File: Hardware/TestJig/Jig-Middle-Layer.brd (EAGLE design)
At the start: 62.2 x 54.6 mm, 8 parts

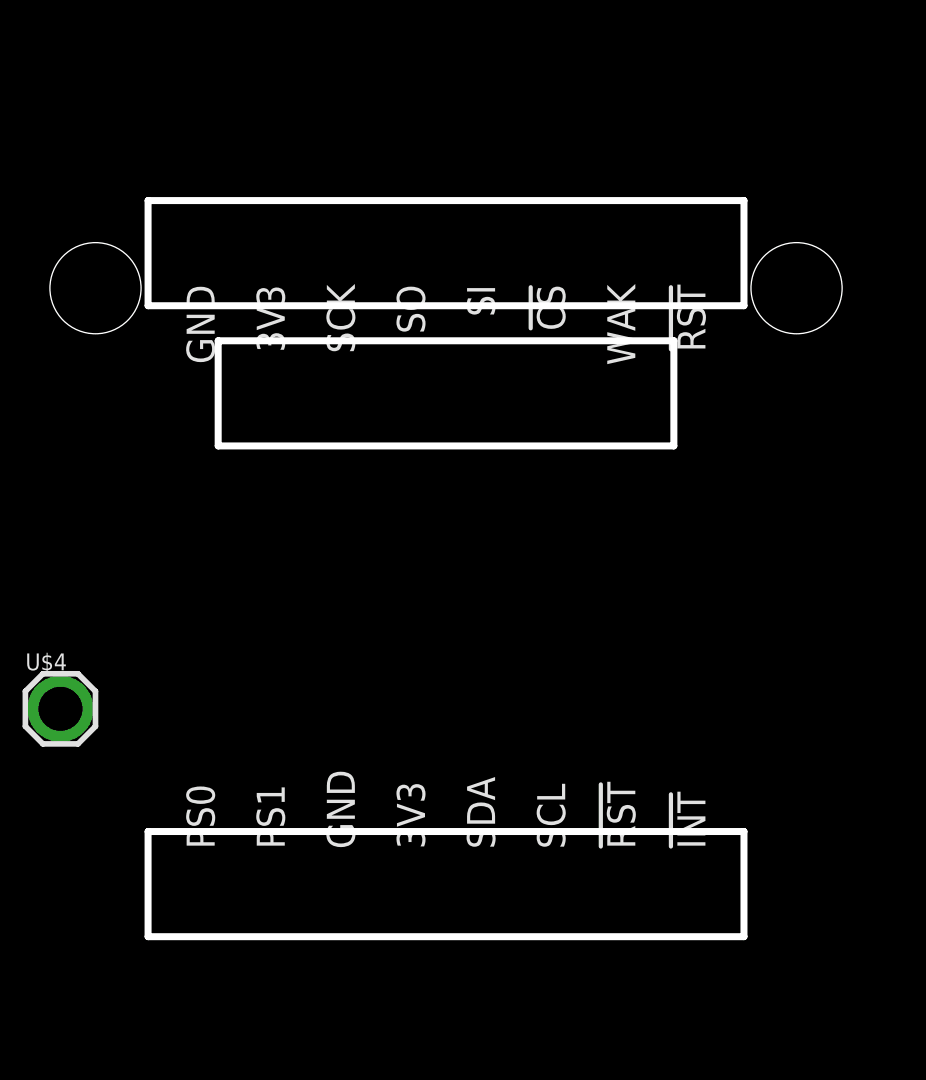
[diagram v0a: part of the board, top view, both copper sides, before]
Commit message: fixed white wires on lower layer, added pass throughs for pogo
replaced white wires with bottom traces. 3  traces:  A4, A5, CS

added PTH holes with 1.45mm diameter, giving .15mm clearance of the pogo pin head.

removed cutouts so PCBs can be fabricated
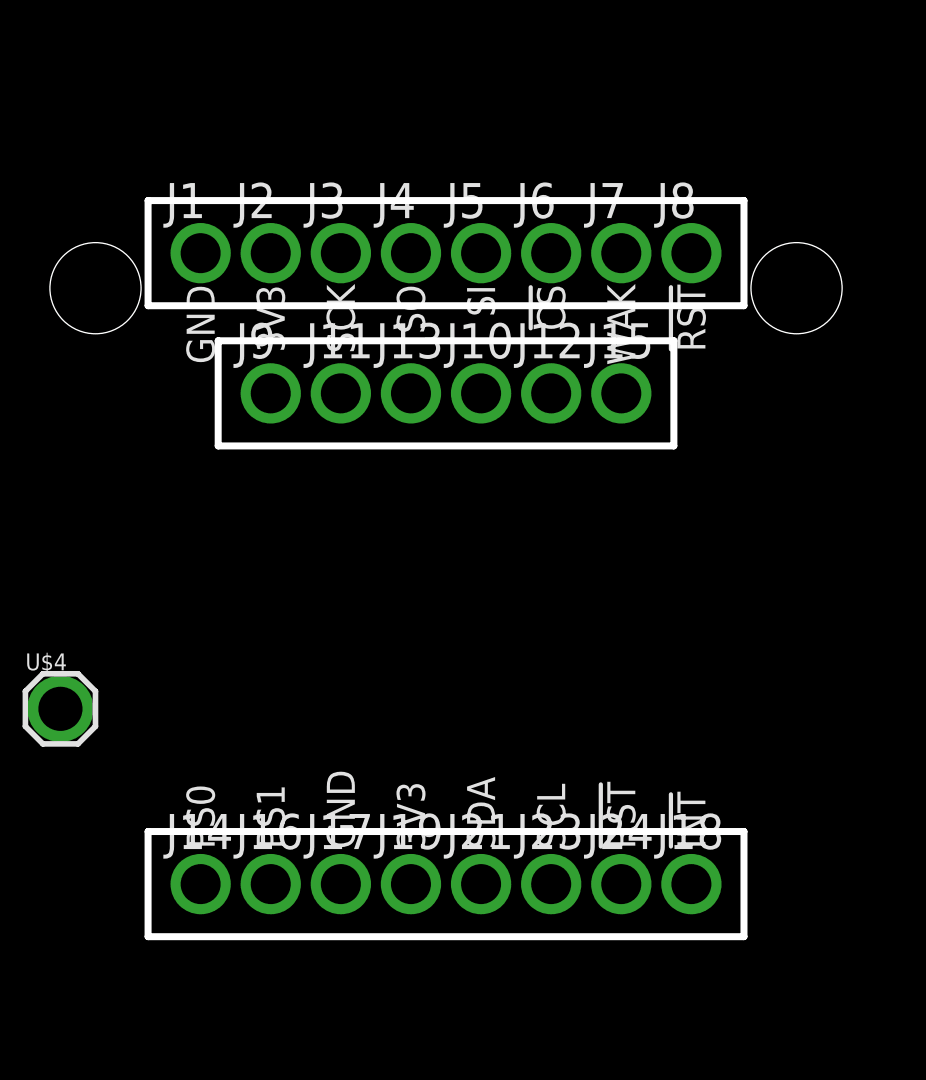
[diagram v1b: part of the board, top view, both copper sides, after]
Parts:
- added J1, J10, J11, J12, J13, J14, J15, J16, J17, J18, J19, J2, J21, J23, J24, J3, J4, J5, J6, J7, J8, J9: POGO_PINTIGHT, KevinKuwata_eagle:POGO_PIN_TIGHT
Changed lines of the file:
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@@
 <setting verticaltext="up"/>
 </settings>
-<grid distance="0.05" unitdist="inch" unit="inch" style="lines" multiple="1" display="yes" altdistance="0.025" altunitdist="inch" altunit="inch"/>
+<grid distance="0.05" unitdist="inch" unit="inch" style="lines" multiple="1" display="yes" altdistance="0.005" altunitdist="inch" altunit="inch"/>
 <layers>
 <layer number="1" name="Top" color="4" fill="1" visible="yes" active="yes"/>
@@
 <layer number="47" name="Measures" color="7" fill="1" visible="no" active="yes"/>
 <layer number="48" name="Document" color="7" fill="1" visible="no" active="yes"/>
-<layer number="49" name="Reference" color="7" fill="1" visible="no" active="yes"/>
+<layer number="49" name="Reference" color="7" fill="1" visible="yes" active="yes"/>
 <layer number="50" name="dxf" color="7" fill="1" visible="no" active="yes"/>
 <layer number="51" name="tDocu" color="6" fill="1" visible="yes" active="yes"/>
@@
 <element name="JP6" library="SparkFun" package="STAND-OFF" value="STAND-OFF" x="2.54" y="2.54"/>
 <element name="U$4" library="Pogo-Footprints" package="1X01_POGO_HEAD" value="POGO_HEAD_11" x="16.51" y="17.78"/>
+<element name="J1" library="KevinKuwata_eagle" package="POGO_PIN_TIGHT" value="POGO_PINTIGHT" x="21.59" y="34.29"/>
+<element name="J2" library="KevinKuwata_eagle" package="POGO_PIN_TIGHT" value="POGO_PINTIGHT" x="24.13" y="34.29"/>
+<element name="J3" library="KevinKuwata_eagle" package="POGO_PIN_TIGHT" value="POGO_PINTIGHT" x="26.67" y="34.29"/>
+<element name="J4" library="KevinKuwata_eagle" package="POGO_PIN_TIGHT" value="POGO_PINTIGHT" x="29.21" y="34.29"/>
+<element name="J5" library="KevinKuwata_eagle" package="POGO_PIN_TIGHT" value="POGO_PINTIGHT" x="31.75" y="34.29"/>
+<element name="J6" library="KevinKuwata_eagle" package="POGO_PIN_TIGHT" value="POGO_PINTIGHT" x="34.29" y="34.29"/>
+<element name="J7" library="KevinKuwata_eagle" package="POGO_PIN_TIGHT" value="POGO_PINTIGHT" x="36.83" y="34.29"/>
+<element name="J8" library="KevinKuwata_eagle" package="POGO_PIN_TIGHT" value="POGO_PINTIGHT" x="39.37" y="34.29"/>
+<element name="J9" library="KevinKuwata_eagle" package="POGO_PIN_TIGHT" value="POGO_PINTIGHT" x="24.13" y="29.21"/>
+<element name="J10" library="KevinKuwata_eagle" package="POGO_PIN_TIGHT" value="POGO_PINTIGHT" x="31.75" y="29.21"/>
+<element name="J11" library="KevinKuwata_eagle" package="POGO_PIN_TIGHT" value="POGO_PINTIGHT" x="26.67" y="29.21"/>
+<element name="J12" library="KevinKuwata_eagle" package="POGO_PIN_TIGHT" value="POGO_PINTIGHT" x="34.29" y="29.21"/>
+<element name="J13" library="KevinKuwata_eagle" package="POGO_PIN_TIGHT" value="POGO_PINTIGHT" x="29.21" y="29.21"/>
+<element name="J14" library="KevinKuwata_eagle" package="POGO_PIN_TIGHT" value="POGO_PINTIGHT" x="21.59" y="11.43"/>
+<element name="J15" library="KevinKuwata_eagle" package="POGO_PIN_TIGHT" value="POGO_PINTIGHT" x="36.83" y="29.21"/>
+<element name="J16" library="KevinKuwata_eagle" package="POGO_PIN_TIGHT" value="POGO_PINTIGHT" x="24.13" y="11.43"/>
+<element name="J17" library="KevinKuwata_eagle" package="POGO_PIN_TIGHT" value="POGO_PINTIGHT" x="26.67" y="11.43"/>
+<element name="J18" library="KevinKuwata_eagle" package="POGO_PIN_TIGHT" value="POGO_PINTIGHT" x="39.37" y="11.43"/>
+<element name="J19" library="KevinKuwata_eagle" package="POGO_PIN_TIGHT" value="POGO_PINTIGHT" x="29.21" y="11.43"/>
+<element name="J21" library="KevinKuwata_eagle" package="POGO_PIN_TIGHT" value="POGO_PINTIGHT" x="31.75" y="11.43"/>
+<element name="J23" library="KevinKuwata_eagle" package="POGO_PIN_TIGHT" value="POGO_PINTIGHT" x="34.29" y="11.43"/>
+<element name="J24" library="KevinKuwata_eagle" package="POGO_PIN_TIGHT" value="POGO_PINTIGHT" x="36.83" y="11.43"/>
 </elements>
 <signals>

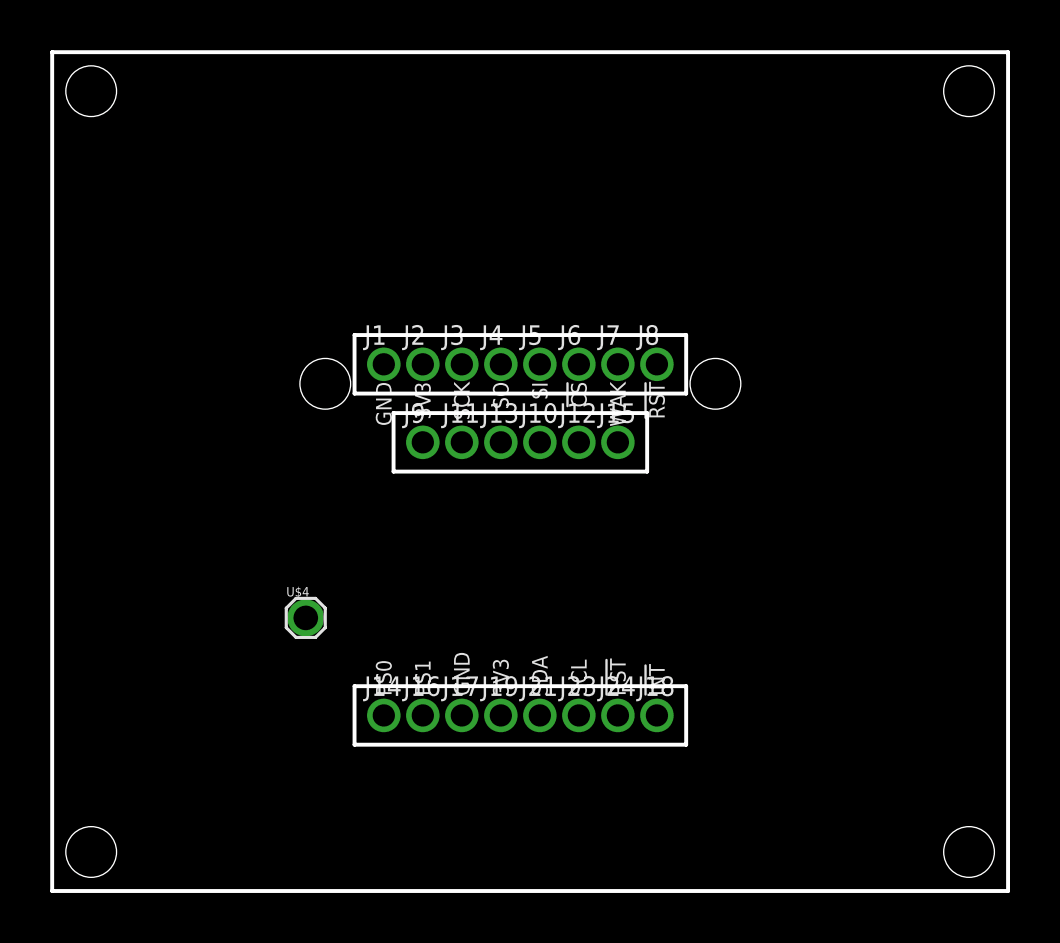
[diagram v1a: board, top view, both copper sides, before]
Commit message: Tweaked testjig middle and top layers
middle layer changes:
-changed holes for the pogopins to pup up through from pads to actual "holes" in eagle file. removed pads from sch and board.
-set hole size to 0.055 inch diameter for optimal lazer cutting in acrylic.

top layer changes:
-tightened up frame to huge product dimensions with 0.016 inch gap.
-added corner cutouts
-added "lift-out" cutout on the side, for easier product removal

Also note, bumped outer dimensions on both middle and top to allow for more strength around the corner standoff holes. Previous deisgn would probably crack if cut in acrylic with lazer.
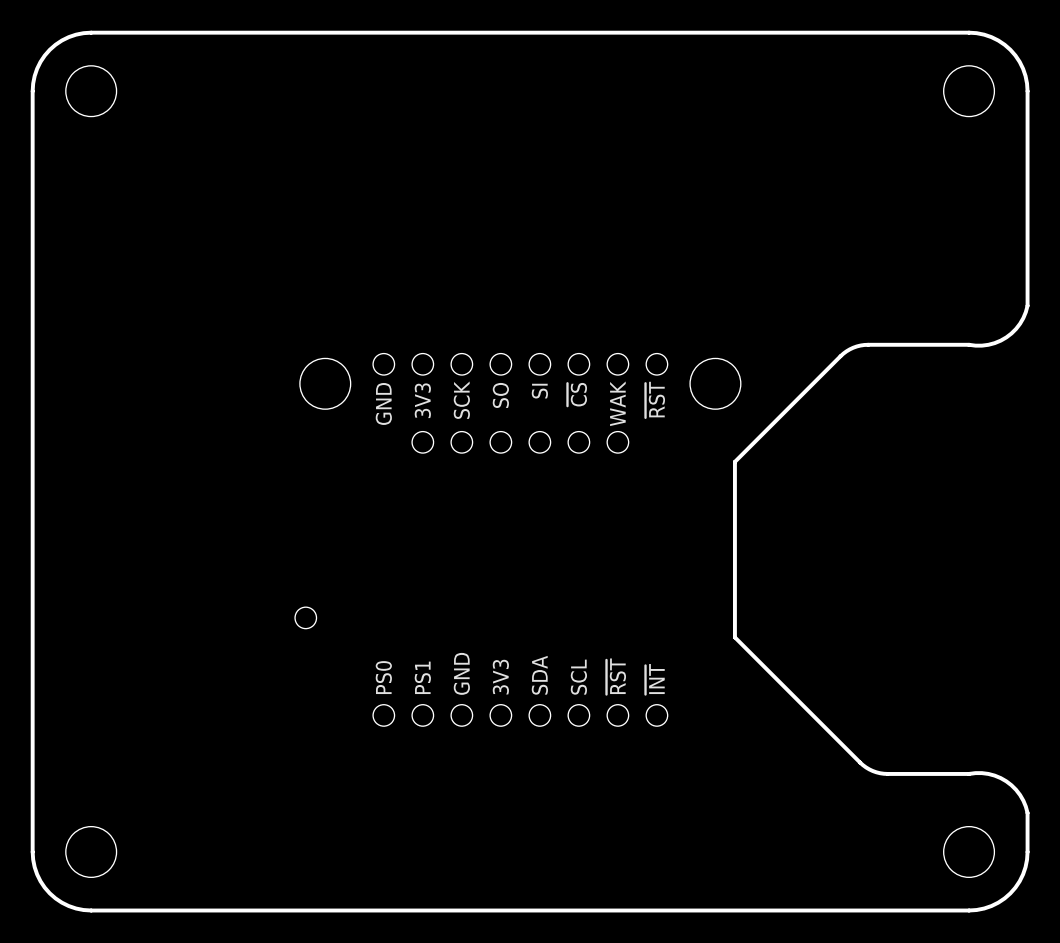
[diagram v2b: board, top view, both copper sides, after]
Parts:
- removed J1, J10, J11, J12, J13, J14, J15, J16, J17, J18, J19, J2, J21, J23, J24, J3, J4, J5, J6, J7, J8, J9: POGO_PINTIGHT, KevinKuwata_eagle:POGO_PIN_TIGHT
- removed U$4: POGO_HEAD_11, Pogo-Footprints:1X01_POGO_HEAD
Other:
- board size 62.2 x 54.6 mm -> 64.8 x 57.2 mm
